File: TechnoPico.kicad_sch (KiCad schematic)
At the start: 158 parts, among them J1 USB_C_Receptacle_USB2.0, J2 Conn_01x02, SW1 Test, SW2 Service, SW3 BOOTSEL, U1 RP2350_60QFN, U2 SN74LV1T34DBV, U3 XC6206PxxxMR, U4 USBLC6-2SC6, Y1 12.000MHz

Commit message: Experimental corner cutouts for mounting
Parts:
- added TP7: EXT LED, TestPoint:TestPoint_Pad_D1.0mm, symbol Connector:TestPoint
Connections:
- net LED_EXT: now reaches D35.2 (DOUT)
- net LED_EXT: now also TP7.1
- no-connect marks 52 -> 51
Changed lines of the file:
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@@
 	)
 	(no_connect
-		(at 271.78 214.63)
-	)
-	(no_connect
 		(at 41.91 68.58)
 	)
@@
 	(wire
 		(pts
+			(xy 48.26 180.34) (xy 48.26 184.15)
+		)
+		(stroke
+			(width 0)
+			(type default)
+		)
+	)
+	(wire
+		(pts
 			(xy 101.6 26.67) (xy 92.71 26.67)
 		)
@@
 		)
 	)
+	(label "LED_EXT"
+		(at 48.26 184.15 90)
+		(fields_autoplaced yes)
+		(effects
+			(font
+				(size 0.635 0.635)
+			)
+			(justify left bottom)
+		)
+	)
 	(label "USB D-"
 		(at 68.58 173.99 90)
@@
 		)
 	)
+	(global_label "LED_EXT"
+		(shape input)
+		(at 271.78 214.63 0)
+		(fields_autoplaced yes)
+		(effects
+			(font
+				(size 1.27 1.27)
+			)
+			(justify left)
+		)
+		(property "Intersheetrefs" "${INTERSHEET_REFS}"
+			(at 282.506 214.63 0)
+			(effects
+				(font
+					(size 1.27 1.27)
+				)
+				(justify left)
+				(hide yes)
+			)
+		)
+	)
 	(global_label "LED_ZONE3"
 		(shape input)
@@
 					(unit 1)
 				)
+			)
+		)
+	)
+	(symbol
+		(lib_id "Connector:TestPoint")
+		(at 48.26 180.34 0)
+		(unit 1)
+		(exclude_from_sim no)
+		(in_bom yes)
+		(on_board yes)
+		(dnp no)
+		(property "Reference" "TP7"
+			(at 49.276 177.292 0)
+			(effects
+				(font
+					(size 1.27 1.27)
+				)
+				(justify left)
+			)
+		)
+		(property "Value" "EXT LED"
+			(at 49.276 179.832 0)
+			(effects
+				(font
+					(size 1.27 1.27)
+				)
+				(justify left)
+			)
+		)
+		(property "Footprint" "TestPoint:TestPoint_Pad_D1.0mm"
+			(at 53.34 180.34 0)
+			(effects
+				(font
+					(size 1.27 1.27)
+				)
+				(hide yes)
+			)
+		)
+		(property "Datasheet" "~"
+			(at 53.34 180.34 0)
+			(effects
+				(font
+					(size 1.27 1.27)
+				)
+				(hide yes)
+			)
+		)
+		(property "Description" "test point"
+			(at 48.26 180.34 0)
+			(effects
+				(font
+					(size 1.27 1.27)
+				)
+				(hide yes)
+			)
+		)
+		(pin "1"
+		)
+		(instances
+			(project "TechnoPico"
+				(path "/1438bc10-a9ef-4a0f-9a48-ff7218bb9654"
+					(reference "TP7")
+					(unit 1)
+				)

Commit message: Add flash
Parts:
- added C50: 100nF, Capacitor_SMD:C_0402_1005Metric, symbol Device:C_Small
- added C51: 100nF, Capacitor_SMD:C_0402_1005Metric_Pad0.74x0.62mm_HandSolder, symbol Device:C_Small
- added D40, D41: WHITE, LED_SMD:LED_0603_1608Metric, symbol Device:LED_Small
- added F1: 6V 0.5A, Fuse:Fuse_0603_1608Metric, symbol Device:Polyfuse_Small
- added J3: Conn_01x04, Connector_PinHeader_1.27mm:PinHeader_1x04_P1.27mm_Vertical, symbol Connector_Generic:Conn_01x04
- added R10: DNF, Resistor_SMD:R_0402_1005Metric_Pad0.72x0.64mm_HandSolder, symbol Device:R_Small
- added R8, R9: 220R, Resistor_SMD:R_0402_1005Metric, symbol Device:R_Small
- added TP8: BOOTSEL, TestPoint:TestPoint_Pad_D1.0mm, symbol Connector:TestPoint
- added U5: W25Q32JVZP, Package_SON:WSON-8-1EP_6x5mm_P1.27mm_EP3.4x4.3mm, symbol Memory_Flash:W25Q32JVZP
- C1, C10, C11, C12, C13, C14, C15, C16, C17, C18, C2, C3, C4, C40, C41, C42, C43, C44, C45, C5, C6, C7, C8, C9: LCSC C437555 -> C15008
- C19: LCSC C1525 -> C1581
- C20, C21: LCSC (none) -> C52923
- C24, C25, C26, C28: LCSC (none) -> C274416
- C27, C29, C30, C31, C32, C33, C34, C35, C36, C37, C38, C46, C47, C48, C49: LCSC (none) -> C1581
- C39: LCSC C12530 -> C15008
- C52, C53, C54, C55: LCSC (none) -> C15008
- D1, D10, D11, D12, D13, D14, D15, D16, D17, D18, D19, D2, D20, D3, D36, D37, D38, D39, D4, D5, D6, D7, D8, D9: LCSC (none) -> C81598
- D21, D22, D23, D24, D25, D26, D27, D28, D29, D30, D31, D32, D33, D34, D35, LED1, LED10, LED11, LED12, LED13, LED14, LED15, LED16, LED17, LED18, LED19, LED2, LED20, LED21, LED22, LED23, LED24, LED3, LED4, LED5, LED6, LED7, LED8, LED9: Designer Notes (none) -> Buy from digikey/etc, place by hand; now not fitted
- J2: Designer Notes (none) -> Optional, surface mount pads, no pins needed; now not fitted
- L1: footprint Inductor_SMD:L_0805_2012Metric -> PA4335.XXXNLT:PA4335.XXXNLT; Designer Notes (none) -> Buy from digikey/etc, place by hand; now not fitted
- MX1, MX10, MX11, MX12, MX13, MX14, MX15, MX16, MX17, MX18, MX2, MX3, MX4, MX5, MX6, MX7, MX8, MX9: Designer Notes (none) -> Buy from your preferred shop, place by hand; now not fitted
- R6: LCSC (none) -> C138002
- R7: LCSC (none) -> C106235
- SW1, SW2: Designer Notes (none) -> Through-hole part, solder by hand; now not fitted
- SW3: LCSC (none) -> C318884
- TP1, TP2, TP3, TP4, TP5, TP6, TP7: Designer Notes (none) -> Test pad, no component to solder; now not fitted
- U3: LCSC (none) -> C5446
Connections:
- net +3V3: now also C51.1, R10.1, R9.1, U5.8 (VCC)
- net +5V: now also C50.1, F1.1, R8.1; no longer C21.1, U3.3 (VI)
- net BOOTSEL: now also TP8.1
- net GND: now also C50.2, C51.2, D40.1 (K), D41.1 (K), U5.4 (GND), U5.9 (EP)
- net SPI_RX: now reaches U1.27 (GPIO16)
- net SPI_RX: now also J3.1 (Pin_1)
- net SPI_CS: now reaches U1.28 (GPIO17)
- net SPI_CS: now also J3.2 (Pin_2)
- net SPI_SCK: now reaches U1.29 (GPIO18)
- net SPI_SCK: now also J3.3 (Pin_3)
- net SPI_TX: now reaches U1.31 (GPIO19)
- net SPI_TX: now also J3.4 (Pin_4)
- net QSPI_SD3: now reaches U1.55 (QSPI_SD3)
- net QSPI_SD3: now also U5.7 (IO3)
- net QSPI_SCLK: now reaches U1.56 (QSPI_SCLK)
- net QSPI_SCLK: now also U5.6 (CLK)
- net QSPI_SD0: now reaches U1.57 (QSPI_SD0)
- net QSPI_SD0: now also U5.5 (DI(IO0))
- net QSPI_SD2: now reaches U1.58 (QSPI_SD2)
- net QSPI_SD2: now also U5.3 (IO2)
- net QSPI_SD1: now reaches U1.59 (QSPI_SD1)
- net QSPI_SD1: now also U5.2 (DO(IO1))
- net QSPI_SS: now reaches R7.2, U1.60 (QSPI_SS)
- net QSPI_SS: now also R10.2, U5.1 (~{CS})
- new net: C21.1, F1.2, U3.3 (VI)
- new net: D41.2 (A), R8.2
- new net: D40.2 (A), R9.2
- no-connect marks 51 -> 42
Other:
- note added: "Flash Memory"
- note added: "INTENDED FOR RP2354, EXTERNAL FLASH JUST IN CASE"
- note added: "POST-REGULATOR 3V3 POWER INDICATOR"
- note added: "PRE-REGULATOR USB POWER INDICATOR"
- note removed: "INTENDED FOR RP2354, NO EXTERNAL FLASH"

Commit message: Reroute 5V to LEDs to split up the ground plane less, etc
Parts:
- removed TP2: GND, TestPoint:TestPoint_Pad_D1.0mm, symbol Connector:TestPoint
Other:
- added sheet Extra Lights (untitled.kicad_sch)
- note added: "SPI FLASH"
- note removed: "Flash Memory"
- moved on the sheet: C39, C40, C41, C42, C43, C44, C45, C51, D21, D22, D23, D24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

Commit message: Finishing touches
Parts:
- C19, C27, C29, C30, C31, C32, C33, C34, C35, C36, C37, C38, C46, C47, C48, C49, C50: LCSC C1581 -> C1525
- C22, C23, C51: footprint Capacitor_SMD:C_0402_1005Metric_Pad0.74x0.62mm_HandSolder -> Capacitor_SMD:C_0402_1005Metric
- R10: now not fitted
- U1: LCSC (none) -> C42411118
- U5: LCSC (none) -> C571260
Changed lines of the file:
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@@
 			)
 		)
-		(property "LCSC" "C1581"
+		(property "LCSC" "C1525"
 			(at 83.82 22.86 0)
 			(effects
@@
 			)
 		)
-		(property "LCSC" "C1581"
+		(property "LCSC" "C1525"
 			(at 101.6 22.86 0)
 			(effects
@@
 			)
 		)
-		(property "LCSC" "C1581"
+		(property "LCSC" "C1525"
 			(at 110.49 166.37 0)
 			(effects
@@
 			)
 		)
-		(property "LCSC" "C1581"
+		(property "LCSC" "C1525"
 			(at 66.04 22.86 0)
 			(effects
@@
 			)
 		)
-		(property "Footprint" "Capacitor_SMD:C_0402_1005Metric_Pad0.74x0.62mm_HandSolder"
+		(property "Footprint" "Capacitor_SMD:C_0402_1005Metric"
 			(at 187.96 158.75 0)
 			(effects
@@
 			)
 		)
-		(property "LCSC" "C1581"
+		(property "LCSC" "C1525"
 			(at 128.27 22.86 0)
 			(effects
@@
 		(in_bom yes)
 		(on_board yes)
-		(dnp no)
+		(dnp yes)
 		(property "Reference" "R10"
 			(at 144.018 46.482 90)
@@
 			)
 		)
-		(property "LCSC" "C1581"
+		(property "LCSC" "C1525"
 			(at 48.26 22.86 0)
 			(effects
@@
 			)
 		)
+		(property "LCSC" "C571260"
+			(at 152.4 58.42 0)
+			(effects
+				(font
+					(size 1.27 1.27)
+				)
+				(hide yes)
+			)
+		)
 		(pin "3"
 		)
@@
 			)
 		)
-		(property "LCSC" "C1581"
+		(property "LCSC" "C1525"
 			(at 92.71 22.86 0)
 			(effects
@@
 			)
 		)
-		(property "LCSC" "C1581"
+		(property "LCSC" "C1525"
 			(at 22.86 176.53 0)
 			(effects
@@
 			)
 		)
-		(property "LCSC" "C1581"
+		(property "LCSC" "C1525"
 			(at 275.59 146.05 0)
 			(effects
@@
 			)
 		)
-		(property "LCSC" "C1581"
+		(property "LCSC" "C1525"
 			(at 137.16 22.86 0)
 			(effects
@@
 			)
 		)
-		(property "LCSC" "C1581"
+		(property "LCSC" "C1525"
 			(at 29.21 22.86 0)
 			(effects
@@
 			)
 		)
-		(property "Footprint" "Capacitor_SMD:C_0402_1005Metric_Pad0.74x0.62mm_HandSolder"
+		(property "Footprint" "Capacitor_SMD:C_0402_1005Metric"
 			(at 162.56 46.99 0)
 			(effects
@@
 			)
 		)
-		(property "Footprint" "Capacitor_SMD:C_0402_1005Metric_Pad0.74x0.62mm_HandSolder"
+		(property "Footprint" "Capacitor_SMD:C_0402_1005Metric"
 			(at 185.42 146.05 0)
 			(effects
@@
 			)
 		)
+		(property "LCSC" "C42411118"
+			(at 73.66 81.28 0)
+			(effects
+				(font
+					(size 1.27 1.27)
+				)
+				(hide yes)
+			)
+		)
 		(pin "36"
 		)
@@
 			)
 		)
-		(property "LCSC" "C1581"
+		(property "LCSC" "C1525"
 			(at 110.49 22.86 0)
 			(effects
@@
 			)
 		)
-		(property "LCSC" "C1581"
+		(property "LCSC" "C1525"
 			(at 119.38 22.86 0)
 			(effects
@@
 			)
 		)
-		(property "LCSC" "C1581"
+		(property "LCSC" "C1525"
 			(at 27.94 176.53 0)
 			(effects
@@
 			)
 		)
-		(property "LCSC" "C1581"
+		(property "LCSC" "C1525"
 			(at 33.02 176.53 0)
 			(effects
@@
 			)
 		)
-		(property "LCSC" "C1581"
+		(property "LCSC" "C1525"
 			(at 74.93 22.86 0)
 			(effects
@@
 			)
 		)
-		(property "LCSC" "C1581"
+		(property "LCSC" "C1525"
 			(at 17.78 176.53 0)
 			(effects

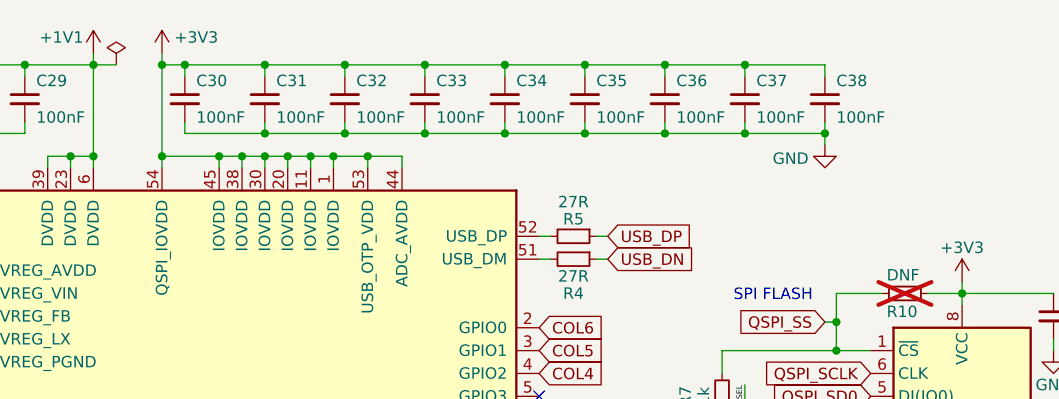
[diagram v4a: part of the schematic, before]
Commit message: Routing changes, use custom RP2350 inductor, etc
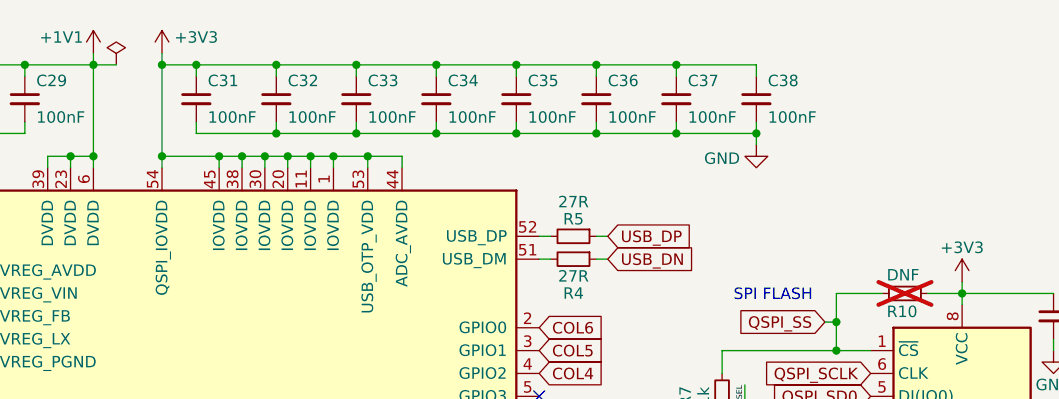
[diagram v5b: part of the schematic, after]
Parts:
- removed C30: 100nF, Capacitor_SMD:C_0402_1005Metric, symbol Device:C_Small
- C25, C26: footprint Capacitor_SMD:C_0402_1005Metric -> RP2350 Components:C_0402_1005Metric_small_pads
- L1: footprint PA4335.XXXNLT:PA4335.XXXNLT -> RP2350 Components:L_pol_2016
- Y1: LCSC C9002 -> C20625731
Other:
- moved on the sheet: C31, C32, C33, C34, C35, C36, C37, C38
